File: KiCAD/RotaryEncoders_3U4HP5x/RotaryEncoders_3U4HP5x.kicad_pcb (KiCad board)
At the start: 2 copper layers, 20.3 x 128.5 mm, 12 parts, among them J1 Conn_01x05_Socket, J2 Conn_01x05_Socket, J3 Conn_01x05_Socket, J4 Conn_01x05_Socket, J5 Conn_01x05_Socket

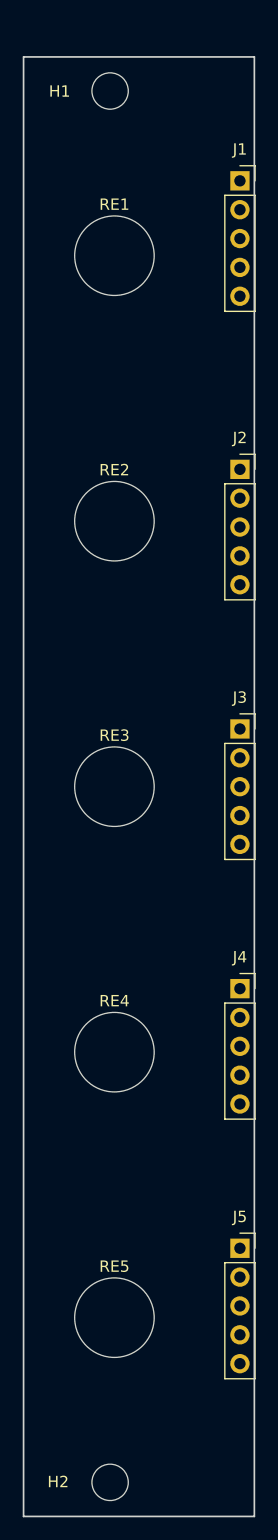
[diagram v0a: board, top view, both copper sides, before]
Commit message: updated PCB widths to better conform to Eurorack standards
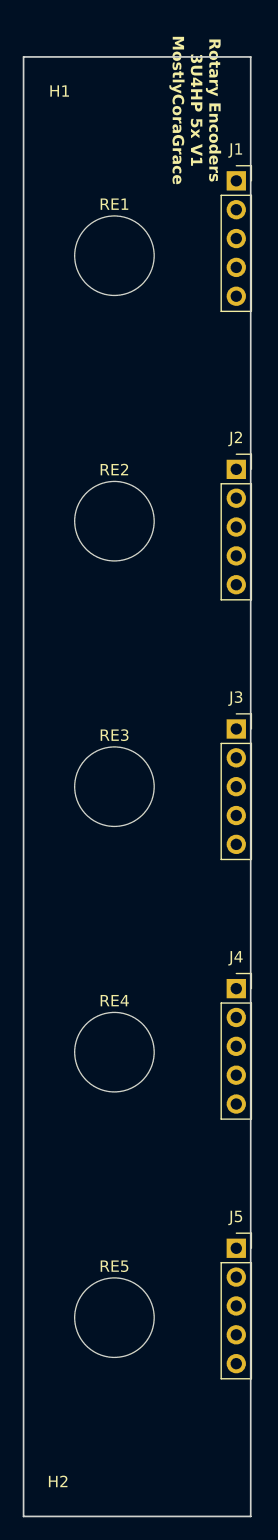
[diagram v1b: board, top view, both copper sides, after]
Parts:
- moved J1 0.32 mm to (18.7, 13.3)
- moved J2 0.32 mm to (18.7, 38.7)
- moved J3 0.32 mm to (18.7, 61.6)
- moved J4 0.32 mm to (18.7, 84.5)
- moved J5 0.32 mm to (18.7, 107.3)
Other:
- board size 20.3 x 128.5 mm -> 20 x 128.5 mm
- board text added: "Rotary Encoders 3U4HP 5x V1 MostlyCoraGrace"

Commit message: removed all front silkscreen, and flipped most modules, to make the boards 'cleaner'.
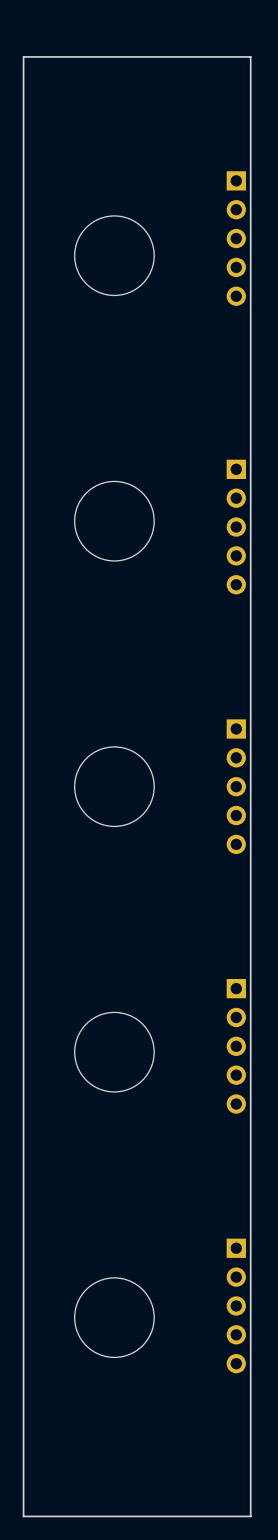
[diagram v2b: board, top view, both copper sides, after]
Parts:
- H1, H2, J1, J2, J3, J4, J5, RE1, RE2, RE3, RE4, RE5: moved to B.Cu
- turned H1 to 180 degrees
- turned H2 to 180 degrees
- turned J1 to 180 degrees
- turned J2 to 180 degrees
- turned J3 to 180 degrees
- turned J4 to 180 degrees
- turned J5 to 180 degrees
- turned RE1 to 180 degrees
- turned RE2 to 180 degrees
- turned RE3 to 180 degrees
- turned RE4 to 180 degrees
- turned RE5 to 180 degrees

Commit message: added copper fills to every module, to maybe possibly increase structural rigidity.
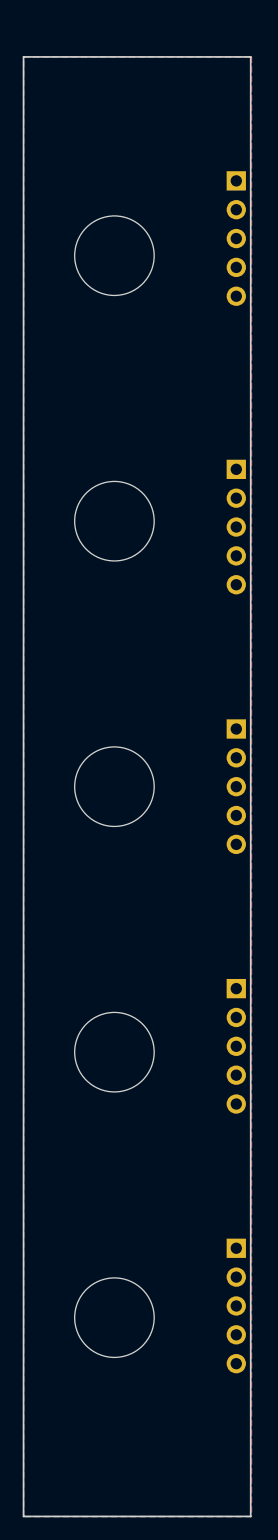
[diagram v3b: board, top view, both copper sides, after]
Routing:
- added copper zone on B.Cu, net (none)
- added copper zone on F.Cu, net (none)
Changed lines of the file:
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@@
+		)
+	)
+	(zone
+		(net 0)
+		(net_name "")
+		(layers "F&B.Cu")
+		(hatch edge 0.5)
+		(connect_pads
+			(clearance 0.5)
+		)
+		(min_thickness 0.25)
+		(filled_areas_thickness no)
+		(fill yes
+			(thermal_gap 0.5)
+			(thermal_bridge_width 0.5)
+			(island_removal_mode 1)
+			(island_area_min 10)
+		)
+		(polygon
+			(pts
+				(xy 0 2.413) (xy 20.066 2.413) (xy 20.066 130.937) (xy 0 130.937)
+			)
 		)
 	)
